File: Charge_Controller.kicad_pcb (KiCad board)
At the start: 2 copper layers, 0 parts

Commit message: Initial Schematic capture DRAFT
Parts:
- added REF**: TO-220-3_Vertical, Package_TO_SOT_THT:TO-220-3_Vertical, F.Cu at (190.2, 121.5)
- added REF**: HTSOP-8-1EP_3.9x4.9mm_P1.27mm_EP2.4x3.2mm_ThermalVias, Package_SO:HTSOP-8-1EP_3.9x4.9mm_P1.27mm_EP2.4x3.2mm_ThermalVias, F.Cu at (179.2, 121.5)
- added REF**: HSOP-8-1EP_3.9x4.9mm_P1.27mm_EP2.41x3.1mm_ThermalVias, Package_SO:HSOP-8-1EP_3.9x4.9mm_P1.27mm_EP2.41x3.1mm_ThermalVias, F.Cu at (168.2, 121.5)
- added REF**: SOP-8_3.76x4.96mm_P1.27mm, Package_SO:SOP-8_3.76x4.96mm_P1.27mm, F.Cu at (168.2, 113.5)
- added REF**: SOP-8-1EP_4.57x4.57mm_P1.27mm_EP4.57x4.45mm, Package_SO:SOP-8-1EP_4.57x4.57mm_P1.27mm_EP4.57x4.45mm, F.Cu at (168.1, 103.4)

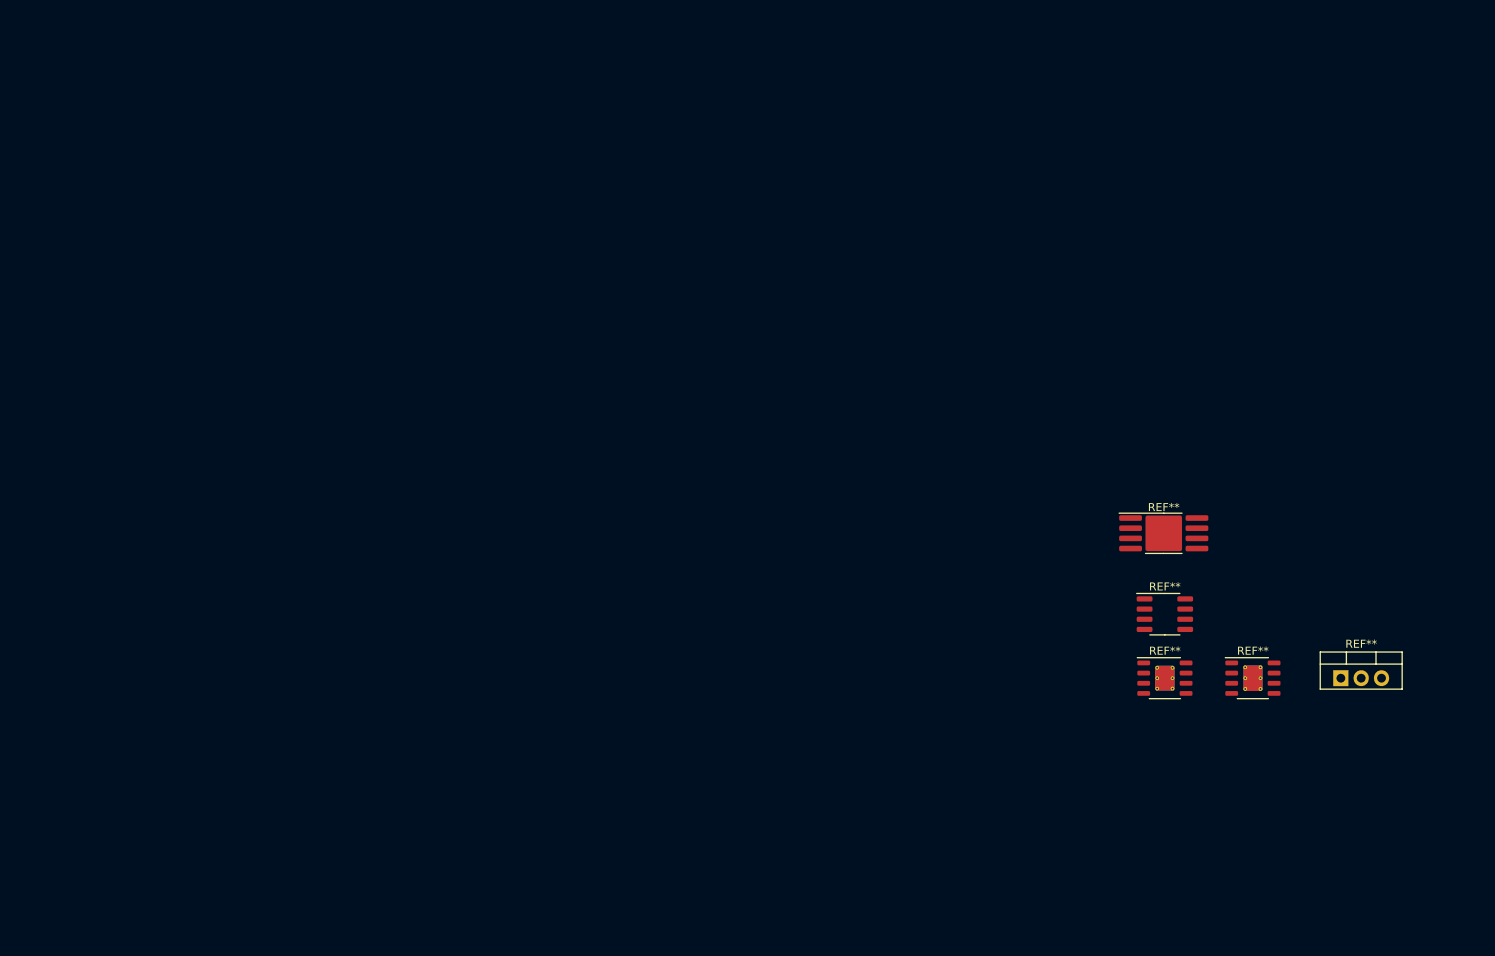
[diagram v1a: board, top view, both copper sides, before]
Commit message: Aligned footprints with JLPCB rotations and offsets, deleted some JLCPCB automation files.
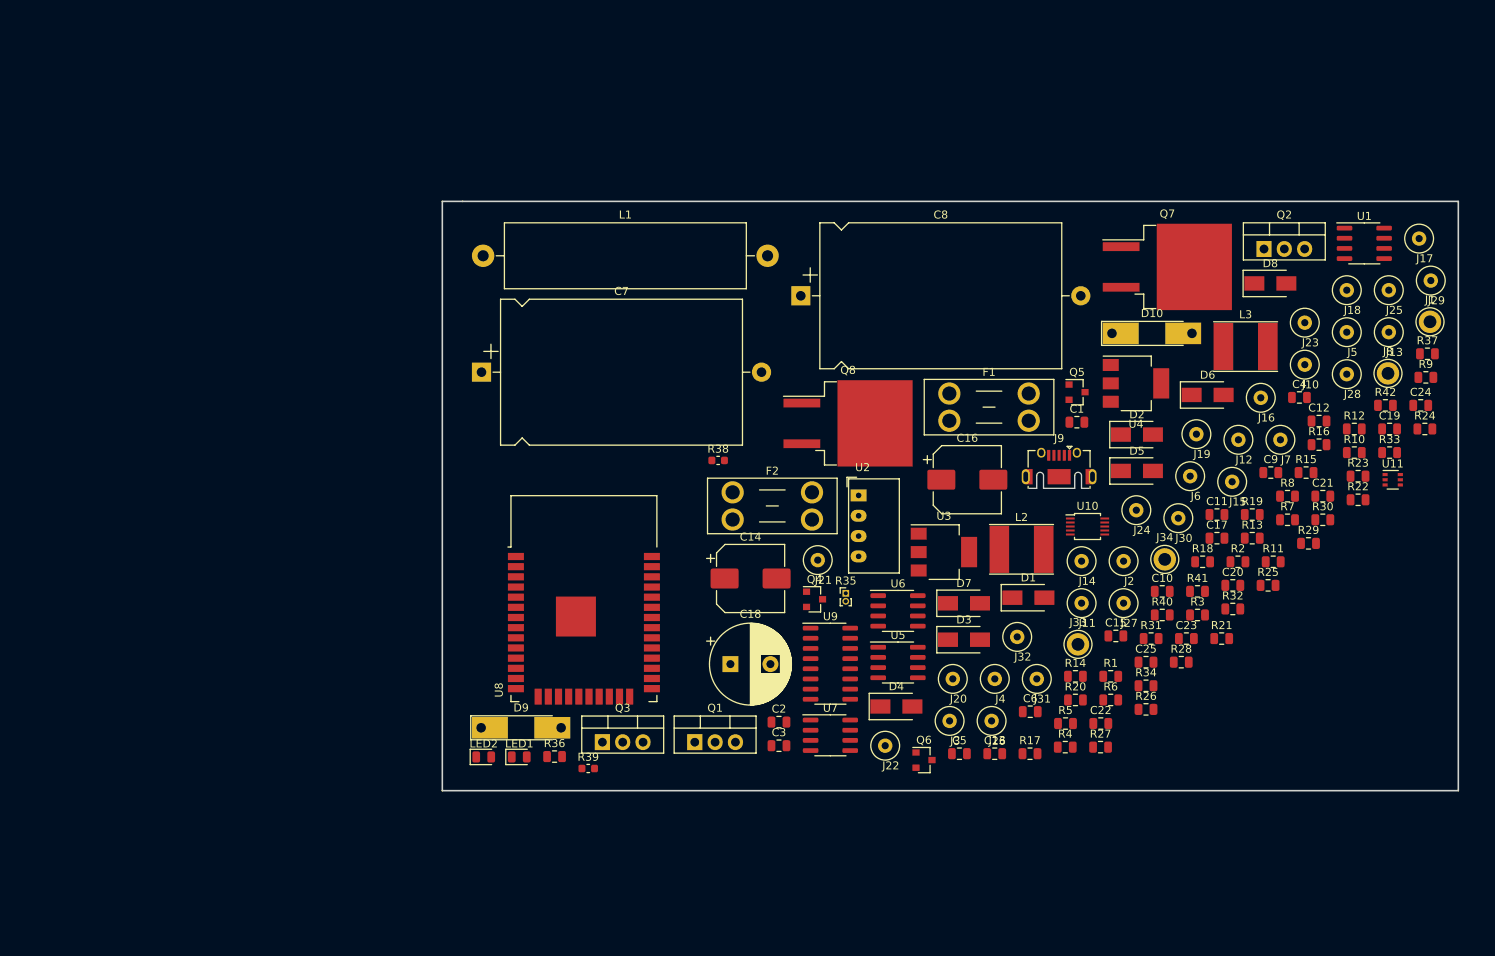
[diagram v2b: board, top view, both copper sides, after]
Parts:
- removed REF**: TO-220-3_Vertical, Package_TO_SOT_THT:TO-220-3_Vertical
- removed REF**: HTSOP-8-1EP_3.9x4.9mm_P1.27mm_EP2.4x3.2mm_ThermalVias, Package_SO:HTSOP-8-1EP_3.9x4.9mm_P1.27mm_EP2.4x3.2mm_ThermalVias
- removed REF**: HSOP-8-1EP_3.9x4.9mm_P1.27mm_EP2.41x3.1mm_ThermalVias, Package_SO:HSOP-8-1EP_3.9x4.9mm_P1.27mm_EP2.41x3.1mm_ThermalVias
- removed REF**: SOP-8_3.76x4.96mm_P1.27mm, Package_SO:SOP-8_3.76x4.96mm_P1.27mm
- removed REF**: SOP-8-1EP_4.57x4.57mm_P1.27mm_EP4.57x4.45mm, Package_SO:SOP-8-1EP_4.57x4.57mm_P1.27mm_EP4.57x4.45mm
- added C1: 100nf, Capacitor_SMD:C_0805_2012Metric, F.Cu at (157.2, 89.5)
- added C10: 10uf, Capacitor_SMD:C_0805_2012Metric, F.Cu at (167.9, 110.7)
- added C11: 100nf, Capacitor_SMD:C_0805_2012Metric, F.Cu at (174.7, 101.0)
- added C12: 100nf, Capacitor_SMD:C_0805_2012Metric, F.Cu at (187.5, 89.4)
- added C13: 100nf, Capacitor_SMD:C_0805_2012Metric, F.Cu at (146.9, 130.9)
- added C14: 100uf, Capacitor_SMD:CP_Elec_8x10, F.Cu at (116.4, 109.0)
- added C15: 33nf, Capacitor_SMD:C_0805_2012Metric, F.Cu at (162.1, 116.2)
- added C16: 100uf, Capacitor_SMD:CP_Elec_8x10, F.Cu at (143.5, 96.7)
- added C17: 33nf, Capacitor_SMD:C_0805_2012Metric, F.Cu at (174.7, 104.0)
- added C18: 4.7uf, Capacitor_THT:CP_Radial_D10.0mm_P5.00mm, F.Cu at (113.9, 119.7)
- added C19: 470nf, Capacitor_SMD:C_0805_2012Metric, F.Cu at (196.3, 90.3)
- added C2: 2.2uf, Capacitor_SMD:C_0805_2012Metric, F.Cu at (120.0, 127.0)
- added C20: 100nf, Capacitor_SMD:C_0805_2012Metric, F.Cu at (176.7, 109.9)
- added C21: 4.7uf, Capacitor_SMD:C_0805_2012Metric, F.Cu at (187.9, 98.8)
- added C22: 4.7uf, Capacitor_SMD:C_0805_2012Metric, F.Cu at (160.2, 127.2)
- added C23: 100nf, Capacitor_SMD:C_0805_2012Metric, F.Cu at (170.9, 116.5)
- added C24: 4.7uf, Capacitor_SMD:C_0805_2012Metric, F.Cu at (200.2, 87.4)
- added C25: 100nf, Capacitor_SMD:C_0805_2012Metric, F.Cu at (165.8, 119.5)
- added C3: 100nf, Capacitor_SMD:C_0805_2012Metric, F.Cu at (120.0, 129.9)
- added C4: 100nf, Capacitor_SMD:C_0805_2012Metric, F.Cu at (185.0, 86.4)
- added C5: 4.7uf, Capacitor_SMD:C_0805_2012Metric, F.Cu at (142.5, 130.9)
- added C6: 4.7uf, Capacitor_SMD:C_0805_2012Metric, F.Cu at (151.4, 125.7)
- added C7: 470uf, Capacitor_THT:CP_Axial_L30.0mm_D18.0mm_P35.00mm_Horizontal, F.Cu at (82.8, 83.2)
- added C8: 470uf, Capacitor_THT:CP_Axial_L30.0mm_D18.0mm_P35.00mm_Horizontal, F.Cu at (122.7, 73.7)
- added C9: 2.2uf, Capacitor_SMD:C_0805_2012Metric, F.Cu at (181.4, 95.8)
- added D1: SS310, Diode_SMD:D_SMA, F.Cu at (151.1, 111.4)
- added D10: D_Zener_Small, Diode_SMD:D_MELF-RM10_Universal_Handsoldering, F.Cu at (166.6, 78.4)
- added D2: SS310, Diode_SMD:D_SMA, F.Cu at (164.7, 91.0)
- added D3: SS310, Diode_SMD:D_SMA, F.Cu at (143.1, 116.7)
- added D4: 1N4007, Diode_SMD:D_SMA, F.Cu at (134.6, 125.0)
- added D5: SS310, Diode_SMD:D_SMA, F.Cu at (164.7, 95.6)
- added D6: SS310, Diode_SMD:D_SMA, F.Cu at (173.5, 86.1)
- added D7: SS310, Diode_SMD:D_SMA, F.Cu at (143.1, 112.1)
- added D8: 1N4007, Diode_SMD:D_SMA, F.Cu at (181.4, 72.2)
- added D9: D_Zener_Small, Diode_SMD:D_MELF-RM10_Universal_Handsoldering, F.Cu at (87.7, 127.7)
- added F1: 35A, Fuse:Fuseholder_Blade_Mini_Keystone_3568, F.Cu at (141.3, 85.9)
- added F2: 35A, Fuse:Fuseholder_Blade_Mini_Keystone_3568, F.Cu at (114.2, 98.3)
- added J1: SOLAR, TestPoint:TestPoint_Keystone_5005-5009_Compact, F.Cu at (201.3, 77.0)
- added J10: Conn_01x01_Female, TestPoint:TestPoint_Loop_D3.50mm_Drill0.9mm_Beaded, F.Cu at (185.7, 82.3)
- added J11: Conn_01x01_Female, TestPoint:TestPoint_Loop_D3.50mm_Drill0.9mm_Beaded, F.Cu at (157.8, 112.1)
- added J12: Conn_01x01_Female, TestPoint:TestPoint_Loop_D3.50mm_Drill0.9mm_Beaded, F.Cu at (177.4, 91.7)
- added J13: Conn_01x01_Female, TestPoint:TestPoint_Loop_D3.50mm_Drill0.9mm_Beaded, F.Cu at (196.2, 78.2)
- added J14: Conn_01x01_Female, TestPoint:TestPoint_Loop_D3.50mm_Drill0.9mm_Beaded, F.Cu at (157.8, 106.9)
- added J15: Conn_01x01_Female, TestPoint:TestPoint_Loop_D3.50mm_Drill0.9mm_Beaded, F.Cu at (176.6, 97.0)
- added J16: Conn_01x01_Female, TestPoint:TestPoint_Loop_D3.50mm_Drill0.9mm_Beaded, F.Cu at (180.2, 86.5)
- added J17: Conn_01x01_Female, TestPoint:TestPoint_Loop_D3.50mm_Drill0.9mm_Beaded, F.Cu at (200.0, 66.5)
- added J18: Conn_01x01_Female, TestPoint:TestPoint_Loop_D3.50mm_Drill0.9mm_Beaded, F.Cu at (190.9, 73.0)
- added J19: Conn_01x01_Female, TestPoint:TestPoint_Loop_D3.50mm_Drill0.9mm_Beaded, F.Cu at (172.1, 91.0)
- added J2: Conn_01x01_Female, TestPoint:TestPoint_Loop_D3.50mm_Drill0.9mm_Beaded, F.Cu at (163.0, 106.9)
- added J20: Conn_01x01_Female, TestPoint:TestPoint_Loop_D3.50mm_Drill0.9mm_Beaded, F.Cu at (141.7, 121.6)
- added J21: Conn_01x01_Female, TestPoint:TestPoint_Loop_D3.50mm_Drill0.9mm_Beaded, F.Cu at (124.8, 106.7)
- added J22: Conn_01x01_Female, TestPoint:TestPoint_Loop_D3.50mm_Drill0.9mm_Beaded, F.Cu at (133.2, 129.9)
- added J23: Conn_01x01_Female, TestPoint:TestPoint_Loop_D3.50mm_Drill0.9mm_Beaded, F.Cu at (185.7, 77.1)
- added J24: Conn_01x01_Female, TestPoint:TestPoint_Loop_D3.50mm_Drill0.9mm_Beaded, F.Cu at (164.6, 100.5)
- added J25: Conn_01x01_Female, TestPoint:TestPoint_Loop_D3.50mm_Drill0.9mm_Beaded, F.Cu at (196.2, 73.0)
- added J26: Conn_01x01_Female, TestPoint:TestPoint_Loop_D3.50mm_Drill0.9mm_Beaded, F.Cu at (146.5, 126.8)
- added J27: Conn_01x01_Female, TestPoint:TestPoint_Loop_D3.50mm_Drill0.9mm_Beaded, F.Cu at (163.0, 112.1)
- added J28: Conn_01x01_Female, TestPoint:TestPoint_Loop_D3.50mm_Drill0.9mm_Beaded, F.Cu at (190.9, 83.5)
- added J29: Conn_01x01_Female, TestPoint:TestPoint_Loop_D3.50mm_Drill0.9mm_Beaded, F.Cu at (201.4, 71.8)
- added J3: Conn_01x01_Female, TestPoint:TestPoint_Loop_D3.50mm_Drill0.9mm_Beaded, F.Cu at (141.3, 126.8)
- added J30: Conn_01x01_Female, TestPoint:TestPoint_Loop_D3.50mm_Drill0.9mm_Beaded, F.Cu at (169.9, 101.5)
- added J31: Conn_01x01_Female, TestPoint:TestPoint_Loop_D3.50mm_Drill0.9mm_Beaded, F.Cu at (152.2, 121.6)
- added J32: Conn_01x01_Female, TestPoint:TestPoint_Loop_D3.50mm_Drill0.9mm_Beaded, F.Cu at (149.7, 116.3)
- added J33: SOLAR, TestPoint:TestPoint_Keystone_5005-5009_Compact, F.Cu at (157.3, 117.3)
- added J34: BATT, TestPoint:TestPoint_Keystone_5005-5009_Compact, F.Cu at (168.2, 106.7)
- added J4: Conn_01x01_Female, TestPoint:TestPoint_Loop_D3.50mm_Drill0.9mm_Beaded, F.Cu at (146.9, 121.6)
- added J5: Conn_01x01_Female, TestPoint:TestPoint_Loop_D3.50mm_Drill0.9mm_Beaded, F.Cu at (190.9, 78.2)
- added J6: Conn_01x01_Female, TestPoint:TestPoint_Loop_D3.50mm_Drill0.9mm_Beaded, F.Cu at (171.4, 96.2)
- added J7: Conn_01x01_Female, TestPoint:TestPoint_Loop_D3.50mm_Drill0.9mm_Beaded, F.Cu at (182.6, 91.7)
- added J8: BATT, TestPoint:TestPoint_Keystone_5005-5009_Compact, F.Cu at (196.1, 83.4)
- added J9: USB_OTG, Connector_USB:USB_Micro-AB_Molex_47590-0001, F.Cu at (155.0, 94.9)
- added L1: 64uH, Inductor_THT:L_Axial_L30.0mm_D8.0mm_P35.56mm_Horizontal_Fastron_77A, F.Cu at (83.0, 68.7)
- added L2: 100uH, Inductor_SMD:L_Taiyo-Yuden_NR-60xx_HandSoldering, F.Cu at (150.3, 105.4)
- added L3: 100uH, Inductor_SMD:L_Taiyo-Yuden_NR-60xx_HandSoldering, F.Cu at (178.3, 80.0)
- added LED1: LED, LED_SMD:LED_0805_2012Metric, F.Cu at (87.5, 131.3)
- added LED2: LED, LED_SMD:LED_0805_2012Metric, F.Cu at (83.0, 131.3)
- added Q1: CSD19505, Package_TO_SOT_THT:TO-220-3_Vertical, F.Cu at (109.4, 129.5)
- added Q2: CSD19505, Package_TO_SOT_THT:TO-220-3_Vertical, F.Cu at (180.6, 67.8)
- added Q3: CSD19505, Package_TO_SOT_THT:TO-220-3_Vertical, F.Cu at (97.9, 129.5)
- added Q4: Si2306, Package_TO_SOT_SMD:SOT-23, F.Cu at (124.4, 111.6)
- added Q5: 2N3904, Package_TO_SOT_SMD:SOT-23, F.Cu at (157.2, 85.8)
- added Q6: 2N3904, Package_TO_SOT_SMD:SOT-23, F.Cu at (138.1, 131.7)
- added Q7: PMOS-100V-90A, Package_TO_SOT_SMD:TO-263-2, F.Cu at (168.5, 70.1)
- added Q8: PMOS-100V-90A, Package_TO_SOT_SMD:TO-263-2, F.Cu at (128.6, 89.7)
- added R1: 200k, Resistor_SMD:R_0805_2012Metric, F.Cu at (161.4, 121.3)
- added R10: 100, Resistor_SMD:R_0805_2012Metric, F.Cu at (191.9, 93.3)
- added R11: 100k, Resistor_SMD:R_0805_2012Metric, F.Cu at (181.7, 107.0)
- added R12: 10k, Resistor_SMD:R_0805_2012Metric, F.Cu at (191.9, 90.3)
- added R13: 10k, Resistor_SMD:R_0805_2012Metric, F.Cu at (179.1, 104.0)
- added R14: 15k, Resistor_SMD:R_0805_2012Metric, F.Cu at (157.0, 121.3)
- added R15: 15k, Resistor_SMD:R_0805_2012Metric, F.Cu at (185.8, 95.8)
- added R16: 1k, Resistor_SMD:R_0805_2012Metric, F.Cu at (187.5, 92.3)
- added R17: 15k, Resistor_SMD:R_0805_2012Metric, F.Cu at (151.3, 130.9)
- added R18: 15k, Resistor_SMD:R_0805_2012Metric, F.Cu at (172.9, 107.0)
- added R19: 1k, Resistor_SMD:R_0805_2012Metric, F.Cu at (179.1, 101.0)
- added R2: 5.1k, Resistor_SMD:R_0805_2012Metric, F.Cu at (177.3, 107.0)
- added R20: 10k, Resistor_SMD:R_0805_2012Metric, F.Cu at (157.0, 124.2)
- added R21: 10k, Resistor_SMD:R_0805_2012Metric, F.Cu at (175.3, 116.5)
- added R22: 10k, Resistor_SMD:R_0805_2012Metric, F.Cu at (192.3, 99.2)
- added R23: 10k, Resistor_SMD:R_0805_2012Metric, F.Cu at (192.3, 96.2)
- added R24: 10k, Resistor_SMD:R_0805_2012Metric, F.Cu at (200.7, 90.3)
- added R25: 10k, Resistor_SMD:R_0805_2012Metric, F.Cu at (181.1, 109.9)
- added R26: 10k, Resistor_SMD:R_0805_2012Metric, F.Cu at (165.8, 125.4)
- added R27: 10k, Resistor_SMD:R_0805_2012Metric, F.Cu at (160.2, 130.1)
- added R28: 10k, Resistor_SMD:R_0805_2012Metric, F.Cu at (170.2, 119.5)
- added R29: 10k, Resistor_SMD:R_0805_2012Metric, F.Cu at (186.2, 104.7)
- added R3: 3.3k, Resistor_SMD:R_0805_2012Metric, F.Cu at (172.3, 113.6)
- added R30: 10k, Resistor_SMD:R_0805_2012Metric, F.Cu at (187.9, 101.7)
- added R31: 10k, Resistor_SMD:R_0805_2012Metric, F.Cu at (166.5, 116.5)
- added R32: 47k, Resistor_SMD:R_0805_2012Metric, F.Cu at (176.7, 112.8)
- added R33: 47k, Resistor_SMD:R_0805_2012Metric, F.Cu at (196.3, 93.3)
- added R34: 1k, Resistor_SMD:R_0805_2012Metric, F.Cu at (165.8, 122.5)
- added R35: 10k_-tc, Connector_PinHeader_1.00mm:PinHeader_1x02_P1.00mm_Vertical, F.Cu at (128.3, 110.9)
- added R36: 10k, Resistor_SMD:R_0805_2012Metric, F.Cu at (91.9, 131.3)
- added R37: 10k, Resistor_SMD:R_0805_2012Metric, F.Cu at (201.0, 81.0)
- added R38: 0R, Resistor_SMD:R_0603_1608Metric, F.Cu at (112.4, 94.3)
- added R39: 0R, Resistor_SMD:R_0603_1608Metric, F.Cu at (96.1, 132.8)
- added R4: 10k, Resistor_SMD:R_0805_2012Metric, F.Cu at (155.8, 130.1)
- added R40: 100k, Resistor_SMD:R_0805_2012Metric, F.Cu at (167.9, 113.6)
- added R41: 1k, Resistor_SMD:R_0805_2012Metric, F.Cu at (172.3, 110.7)
- added R42: 1k, Resistor_SMD:R_0805_2012Metric, F.Cu at (195.8, 87.4)
- added R5: 1k, Resistor_SMD:R_0805_2012Metric, F.Cu at (155.8, 127.2)
- added R6: 10k, Resistor_SMD:R_0805_2012Metric, F.Cu at (161.4, 124.2)
- added R7: 10k, Resistor_SMD:R_0805_2012Metric, F.Cu at (183.5, 101.7)
- added R8: 100k, Resistor_SMD:R_0805_2012Metric, F.Cu at (183.5, 98.8)
- added R9: 100, Resistor_SMD:R_0805_2012Metric, F.Cu at (200.8, 83.9)
- added U1: ACS712-30A, Package_SO:SOIC-8_3.9x4.9mm_P1.27mm, F.Cu at (193.1, 67.2)
- added U10: ADS1015, Package_SO:TSSOP-10_3x3mm_P0.5mm, F.Cu at (158.5, 102.5)
- added U11: NUP4202, Package_TO_SOT_SMD:SOT-363_SC-70-6, F.Cu at (196.7, 96.7)
- added U2: B1212, Converter_DCDC:Converter_DCDC_muRata_CRE1xxxxxxSC_THT, F.Cu at (129.9, 98.7)
- added U3: AMS1117-5.0, Package_TO_SOT_SMD:SOT-223-3_TabPin2, F.Cu at (140.6, 105.7)
- added U4: AMS1117-3.3, Package_TO_SOT_SMD:SOT-223-3_TabPin2, F.Cu at (164.6, 84.7)
- added U5: XL7005A, Package_SO:SOIC-8_3.9x4.9mm_P1.27mm, F.Cu at (134.8, 119.5)
- added U6: XL7005A, Package_SO:SOIC-8_3.9x4.9mm_P1.27mm, F.Cu at (134.8, 113.1)
- added U7: IR2104, Package_SO:SOIC-8_3.9x4.9mm_P1.27mm, F.Cu at (126.4, 128.6)
- added U8: ESP32-WROOM-32, RF_Module:ESP32-WROOM-32, F.Cu at (95.6, 114.5)
- added U9: CH340G, Package_SO:SOIC-16_3.9x9.9mm_P1.27mm, F.Cu at (126.4, 119.7)
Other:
- board outline added: 127 x 73.7 mm
